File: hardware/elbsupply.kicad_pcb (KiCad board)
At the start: 2 copper layers, 74 parts, among them CON1 AVR-ISP-6, IC1 ATMEGA8-AI, P1 OUT_POS, P2 OUT_GND, SW1 SW_L, SW2 SW_R, U1 LM393, U2 TPS54331DDA, U3 LT1490, U4 LM358, U5 TS78L05CS, U6 LT3083

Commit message: binding post distance is now 3/4 inch
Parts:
- added P3: POWER_IN, Connect:bornier2, B.Cu at (52.0, 87.0)
- C1, C12, C13, C14, C15, C16, C17, C18, C19, C2, C20, C21, C22, C23, C24, C25, C26, C27, C3, C4, C5, C6, C7, C8, C9, CON1, D1, D2, D3, D4, D5, IC1, L1, R1, R10, R11, R12, R13, R14, R16, R17, R18, R19, R2, R20, R21, R22, R23, R3, R4, R5, R6, R7, R8, R9, RP1, RP2, RP3, RP4, RP5, RV1, U1, U2, U3, U4, U5, U6: moved to B.Cu
- R15: footprint Resistors_SMD:R_0603_HandSoldering -> devthrash_KICAD:CRA2512-Bourns; moved to B.Cu
- moved U2 220.0 mm to (33.0, 111.0), turned to 180 degrees
- moved U6 181.3 mm to (102.0, 88.0)
- moved RP2 180.6 mm to (41.6, 174.0)
- moved RP4 178.9 mm to (45.6, 181.0)
- moved RP5 171.7 mm to (49.6, 170.0)
- moved RP1 171.6 mm to (47.6, 162.0)
- moved RP3 169.9 mm to (55.6, 182.0)
- moved RV1 168.1 mm to (52.0, 44.0), turned to 90 degrees
- moved C27 163.7 mm to (56.6, 165.0)
- moved C22 163.1 mm to (58.6, 170.0)
- moved R19 158.8 mm to (60.6, 161.0)
- moved R18 158.7 mm to (62.6, 168.0)
- moved P1 155.2 mm to (115.6, 84.5)
- moved R5 153.0 mm to (74.6, 184.0)
- moved C25 151.1 mm to (79.6, 190.0)
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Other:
- board outline added: 105 x 64.4 mm

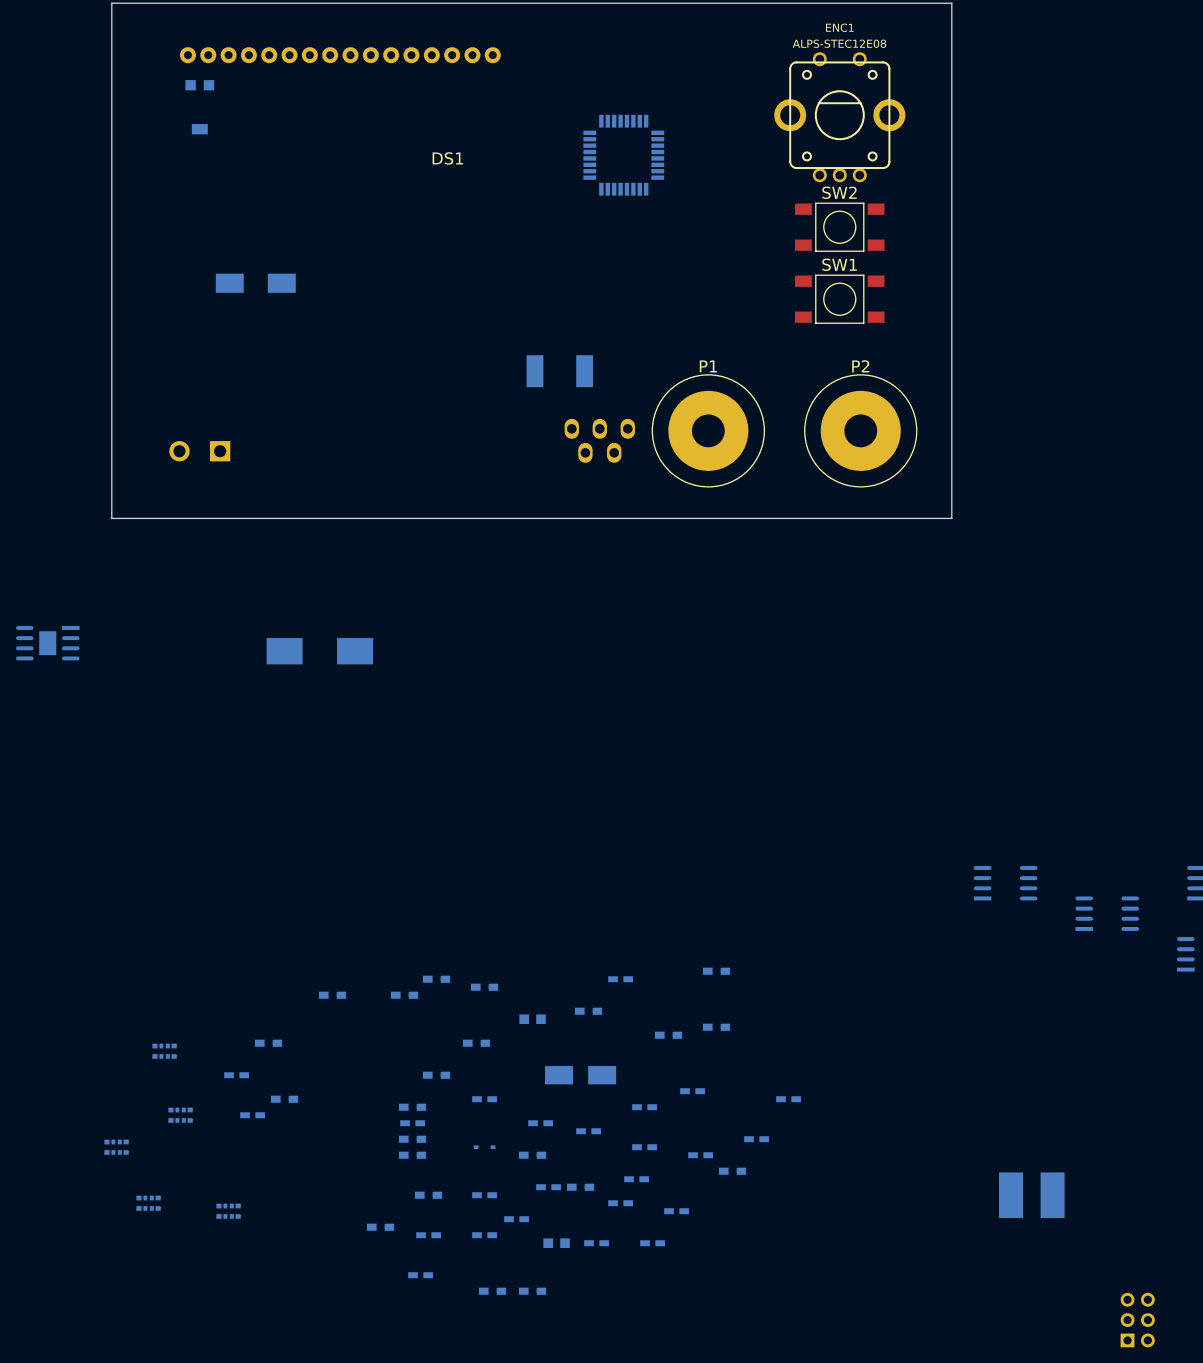
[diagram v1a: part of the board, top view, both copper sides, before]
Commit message: fixed Q1 footprint issues
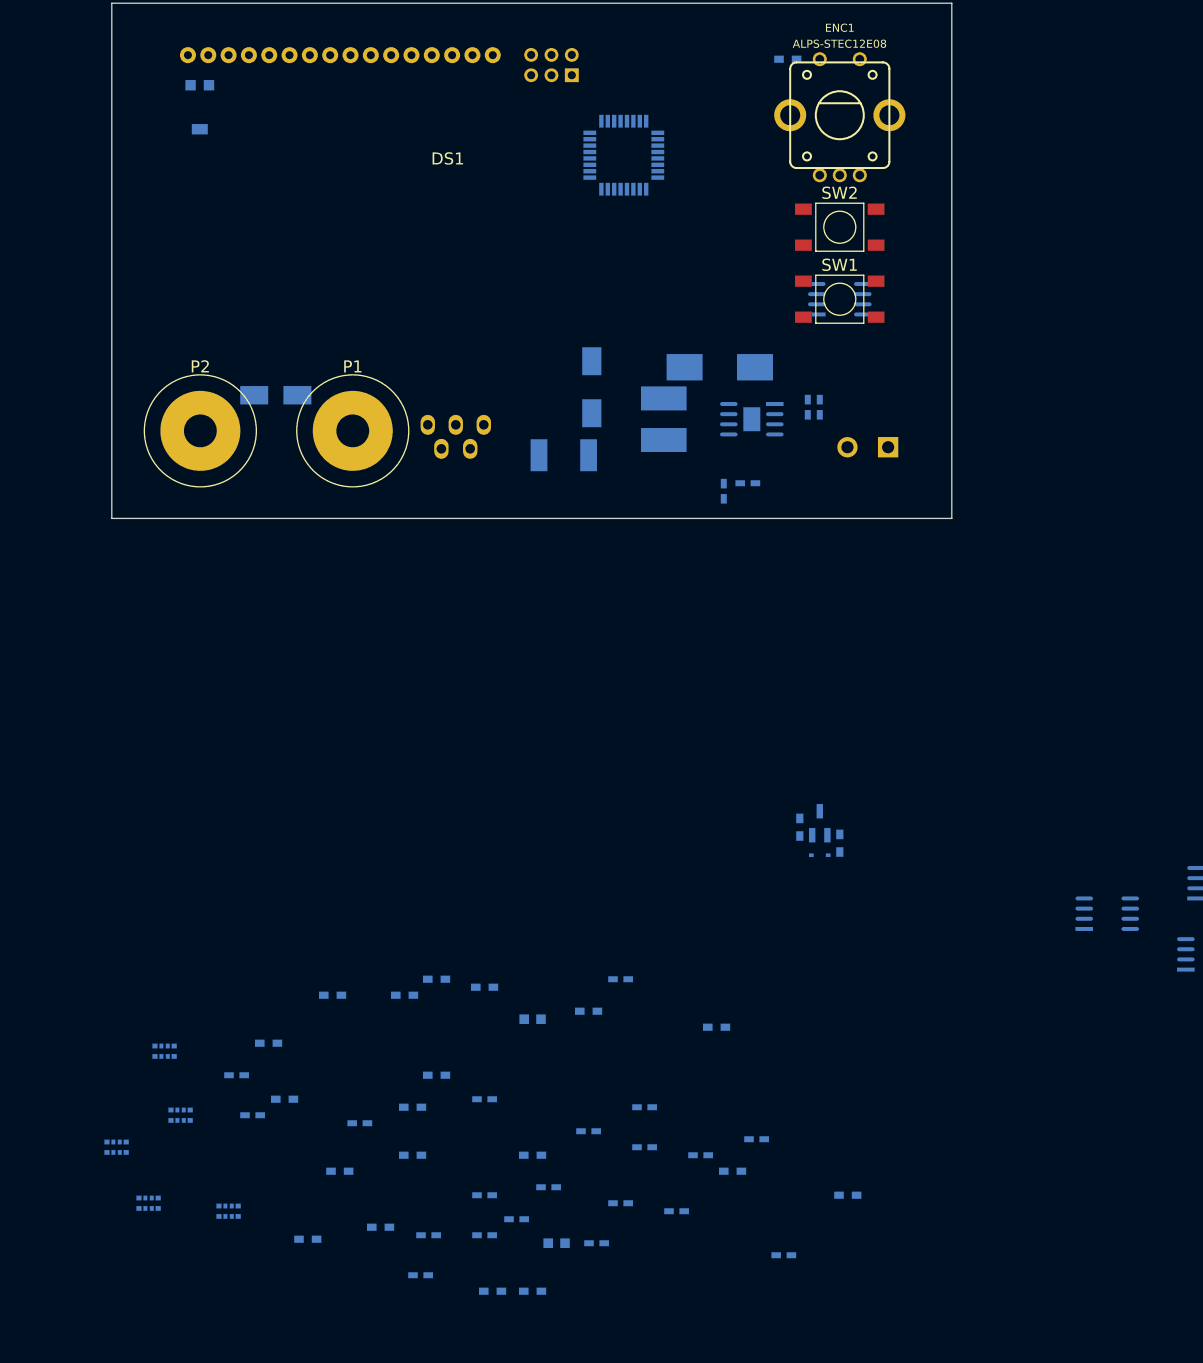
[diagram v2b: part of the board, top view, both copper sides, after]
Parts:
- added Q1: KST2907A, Housings_SOT-23_SOT-143_TSOT-6:SOT23_Handsoldering, B.Cu at (129.5, 133.5)
- moved CON1 172.7 mm to (98.5, 40.0), turned to 90 degrees
- moved R6 129.0 mm to (125.5, 38.0)
- moved L1 107.4 mm to (110.0, 83.0), turned to 270 degrees
- moved C5 95.7 mm to (120.5, 91.0)
- moved D5 93.1 mm to (61.5, 80.0), turned to 180 degrees
- moved U2 92.3 mm to (121.0, 83.0)
- moved C1 86.7 mm to (128.0, 81.5), turned to 90 degrees
- moved C2 86.6 mm to (129.5, 81.5), turned to 90 degrees
- moved P3 83.5 mm to (135.5, 86.5)
- moved P2 82.6 mm to (52.1, 84.5)
- moved C4 82.3 mm to (117.5, 92.0), turned to 270 degrees
- moved U5 75.9 mm to (132.0, 68.0)
- moved D3 61.3 mm to (117.0, 76.5), turned to 180 degrees
- moved D4 55.6 mm to (129.5, 137.5), turned to 180 degrees
- moved P1 44.4 mm to (71.1, 84.5)
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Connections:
- P3 pad 1: +24V -> GND
- P3 pad 2: GND -> +24V

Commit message: continued layout
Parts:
- C6, D1, D2, R2, R23, R3: moved to F.Cu
- moved U1 151.8 mm to (55.8, 60.0)
- moved C25 140.6 mm to (98.5, 50.7), turned to 90 degrees
- moved U4 130.9 mm to (66.7, 58.9)
- moved C27 126.9 mm to (112.3, 51.0), turned to 90 degrees
- moved RP4 125.3 mm to (87.4, 62.9), turned to 180 degrees
- moved C24 122.8 mm to (96.9, 50.7), turned to 270 degrees
- moved U3 121.8 mm to (80.9, 69.4), turned to 270 degrees
- moved RP3 121.1 mm to (79.5, 63.3), turned to 180 degrees
- moved R23 120.5 mm to (85.0, 33.5)
- moved R1 115.3 mm to (125.0, 86.7)
- moved R17 114.5 mm to (83.6, 50.5)
- moved R22 113.0 mm to (105.8, 42.6), turned to 90 degrees
- moved RP5 109.8 mm to (87.5, 66.9)
- moved RP2 106.8 mm to (71.3, 71.4)
- moved RP1 104.9 mm to (83.0, 63.3), turned to 180 degrees
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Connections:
- net Net-(C20-Pad1) renamed /LIN_IN
- net Net-(C26-Pad1) renamed /LIN_OUT
- net Net-(C6-Pad2) renamed /SMPS_SW
- net Net-(C8-Pad1) renamed /SMPS_OUT
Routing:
- net Net-(D4-Pad1): track 0.00 -> 5.05 mm
- net Net-(D4-Pad2): track 0.00 -> 4.25 mm
- net Net-(Q1-Pad3): track 0.00 -> 2.73 mm
- net Net-(C3-Pad2): track 0.00 -> 1.82 mm
- added copper zone on B.Cu, net +24V
- added copper zone on B.Cu, net /LIN_IN
- added copper zone on B.Cu, net /SMPS_OUT
- added copper zone on B.Cu, net /SMPS_SW
- added copper zone on B.Cu, net GND
- added copper zone on F.Cu, net GND

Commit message: parts placement largely finished
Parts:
- R2: moved to B.Cu
- moved C15 143.8 mm to (129.6, 49.0), turned to 270 degrees
- moved C12 143.1 mm to (132.0, 40.4), turned to 180 degrees
- moved R14 142.3 mm to (131.2, 48.8), turned to 270 degrees
- moved R4 138.2 mm to (132.0, 59.2)
- moved R5 135.7 mm to (132.0, 61.0)
- moved C16 135.7 mm to (134.6, 49.0), turned to 90 degrees
- moved R16 129.2 mm to (133.0, 48.8), turned to 270 degrees
- moved C17 126.2 mm to (85.6, 67.6), turned to 180 degrees
- moved C19 123.2 mm to (131.1, 69.7), turned to 90 degrees
- moved C23 119.7 mm to (100.8, 61.0), turned to 180 degrees
- moved C14 118.0 mm to (93.0, 65.0)
- moved C7 117.8 mm to (136.2, 59.2)
- moved R11 116.7 mm to (90.0, 63.8), turned to 90 degrees
- moved C18 110.6 mm to (141.8, 69.4), turned to 90 degrees
- moved R13 109.0 mm to (102.4, 75.4), turned to 270 degrees
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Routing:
- net /I_Meas: track 0.00 -> 23.5 mm
- net /I_Set: track 0.00 -> 13.0 mm
- net /V_control: track 0.00 -> 11.1 mm
- net Net-(R12-Pad1): track 0.00 -> 10.9 mm
- net /SMPS_OUT: track 0.00 -> 7.74 mm
- net Net-(R17-Pad2): track 0.00 -> 6.31 mm
- net /V_Set: track 0.00 -> 6.25 mm
- net Net-(RP2-Pad3): track 0.00 -> 5.37 mm
- net Net-(C6-Pad1): track 0.00 -> 4.08 mm, vias 0 -> 1
- net /LIN_IN: track 0.00 -> 4.04 mm
- net /SMPS_SW: track 0.00 -> 3.90 mm, vias 0 -> 1
- net Net-(RP2-Pad8): track 0.00 -> 2.66 mm
- net Net-(RP1-Pad5): track 0.00 -> 2.00 mm
- net /I_ADC: track 0.00 -> 1.60 mm
- net Net-(RP3-Pad1): track 0.00 -> 0.80 mm
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- added copper zone on B.Cu, net /LIN_OUT

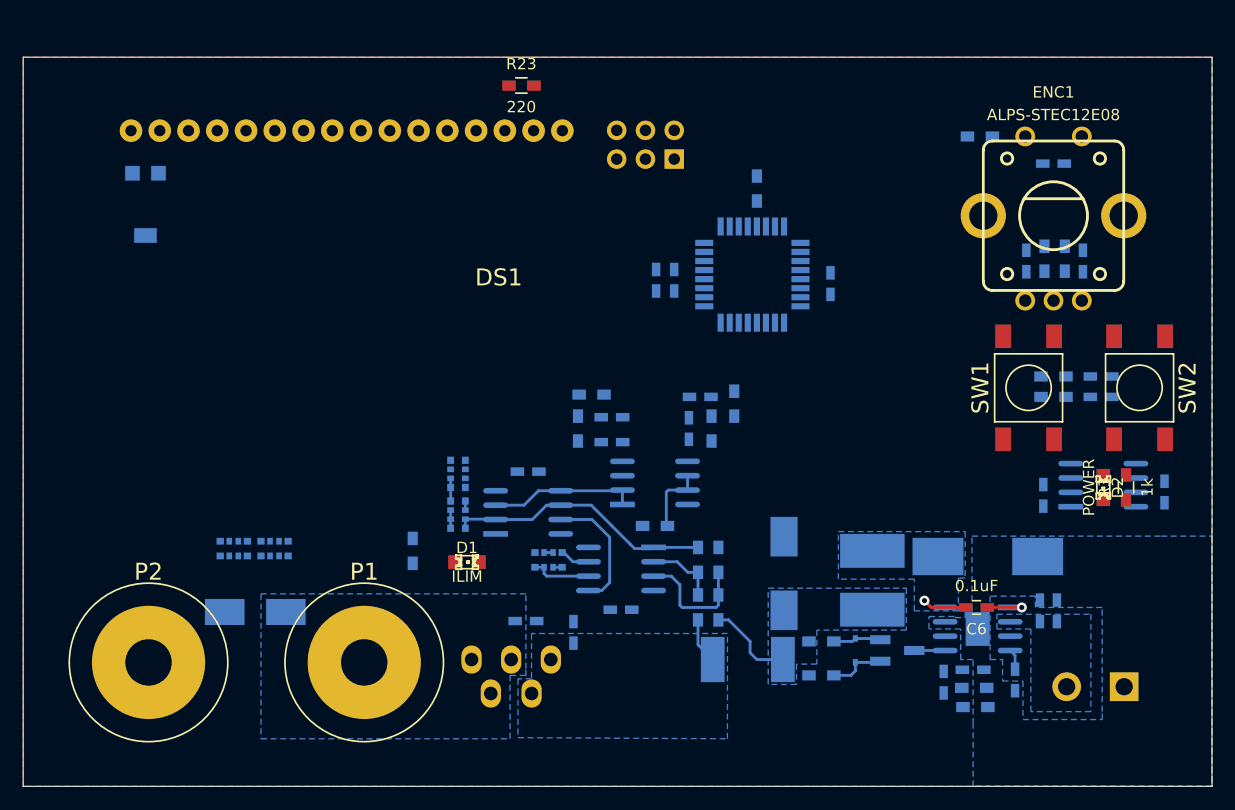
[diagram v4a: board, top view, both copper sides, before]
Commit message: added PCB mounting holes, need repositioning of connectors and LCD
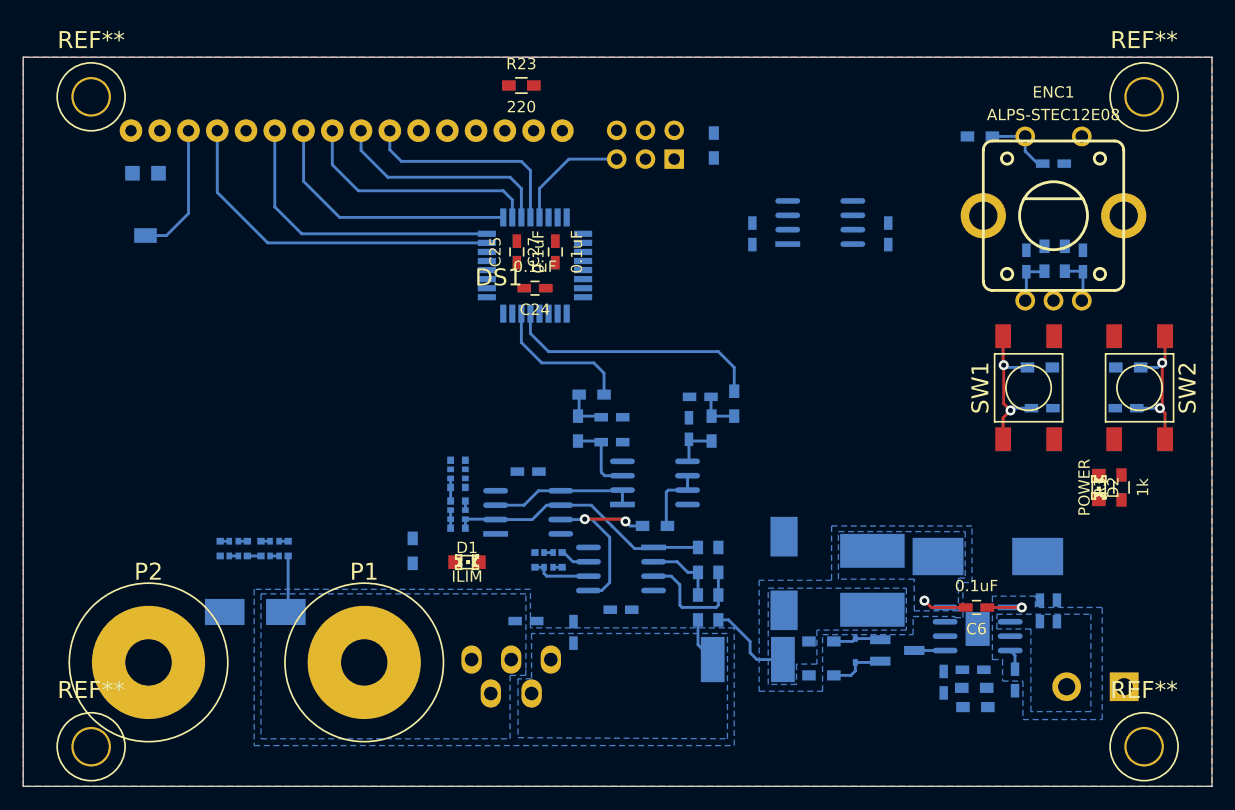
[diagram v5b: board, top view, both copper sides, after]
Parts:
- added REF**: Screw_PAN_Head_M3, devthrash_KICAD:Screw_PAN_Head_M3, F.Cu at (140.0, 34.5)
- added REF**: Screw_PAN_Head_M3, devthrash_KICAD:Screw_PAN_Head_M3, F.Cu at (47.0, 34.5)
- added REF**: Screw_PAN_Head_M3, devthrash_KICAD:Screw_PAN_Head_M3, F.Cu at (47.0, 91.9)
- added REF**: Screw_PAN_Head_M3, devthrash_KICAD:Screw_PAN_Head_M3, F.Cu at (140.0, 91.9)
- C24, C25, C27: moved to F.Cu
- moved C19 34.6 mm to (105.4, 46.6)
- moved U5 34.1 mm to (111.4, 45.6)
- moved C18 33.4 mm to (117.4, 46.6)
- moved C27 24.5 mm to (88.0, 48.2)
- moved IC1 19.2 mm to (86.2, 49.4)
- moved C25 14.1 mm to (84.6, 48.2)
- moved C24 10.7 mm to (86.2, 51.4), turned to 180 degrees
- moved R5 7.09 mm to (138.6, 58.4)
- moved C7 5.91 mm to (131.0, 62.0)
- moved R22 5.37 mm to (102.0, 38.8)
- moved C9 2.42 mm to (138.4, 62.0), turned to 180 degrees
- moved R4 1.44 mm to (130.8, 58.4), turned to 180 degrees
- moved D2 0.40 mm to (136.0, 69.0)
- moved R3 0.40 mm to (138.0, 69.0)
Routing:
- net /LCD_RS: track 0.00 -> 31.1 mm
- net /LCD_E: track 0.00 -> 26.4 mm
- net /LCD_D0: track 0.00 -> 23.4 mm
- net /V_PWM: track 0.00 -> 23.1 mm
- net /LCD_D1: track 0.00 -> 21.7 mm
- net /LCD_D2: track 0.00 -> 19.9 mm
- net /LCD_D3: track 0.00 -> 19.0 mm
- net /SW_L: track 0.00 -> 13.8 mm, vias 0 -> 2
- net /SW_R: track 0.00 -> 13.6 mm, vias 0 -> 2
- net /I_PWM: track 0.00 -> 12.9 mm
- net Net-(DS1-Pad3): track 0.00 -> 11.9 mm
- net /~RST~: track 0.00 -> 10.4 mm
- net Net-(C14-Pad1): track 0.00 -> 6.75 mm
- net /ENC_SW: track 0.00 -> 6.21 mm
- net /V_control: track 11.1 -> 16.6 mm, vias 0 -> 2
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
